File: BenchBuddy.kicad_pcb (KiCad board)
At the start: 4 copper layers, 165.1 x 63.5 mm, 0 parts

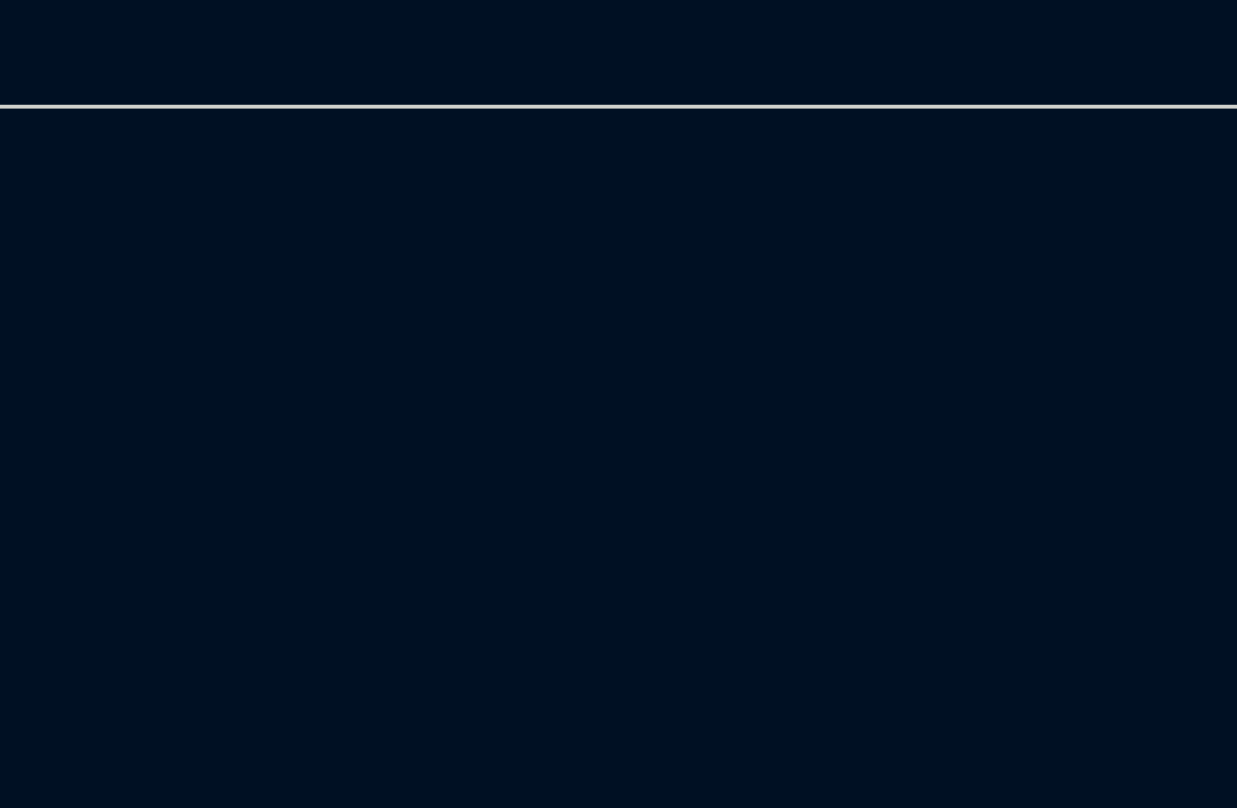
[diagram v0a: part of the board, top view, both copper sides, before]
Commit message: Created Footprints and Placed Relay Module
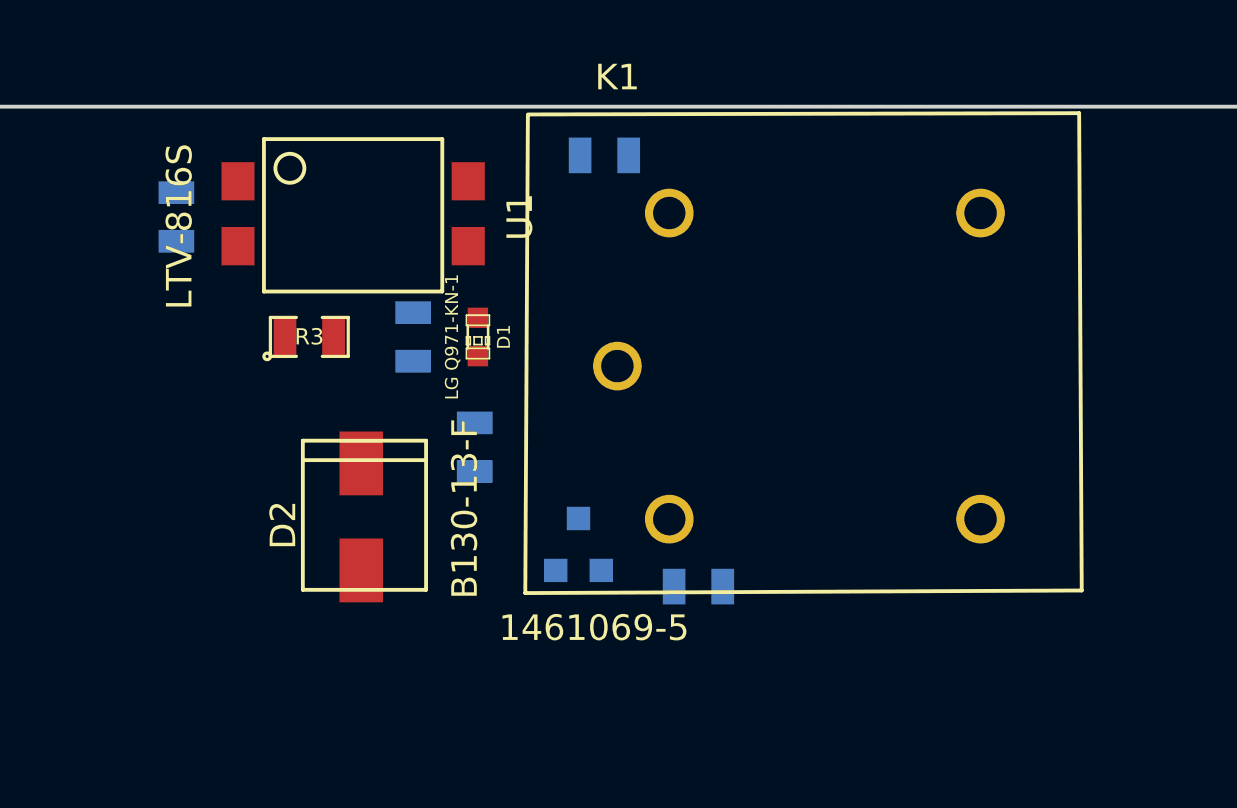
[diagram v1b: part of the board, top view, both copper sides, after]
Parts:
- added D1: LG Q971-KN-1, LED-0603, F.Cu at (264.2, 104.8)
- added D2: B130-13-F, SMA, F.Cu at (259.6, 113.9)
- added K1: 1461069-5, TE-SPDT, F.Cu at (269.6, 105.9)
- added Q1: 2N3904, SOT23EBC, B.Cu at (268.1, 112.9)
- added R1: 500, SM0805, B.Cu at (252.3, 100.1)
- added R2: 200, SM0805, B.Cu at (261.6, 104.8)
- added R3: 0, SM0805, F.Cu at (257.6, 104.8)
- added R4: 100, SM0805, B.Cu at (264.0, 109.1)
- added R5: 0, SM0805, B.Cu at (269.1, 97.7)
- added R6: 0, SM0805, B.Cu at (272.8, 114.6)
- added U1: LTV-816S, 4-SMD, F.Cu at (254.8, 98.7)

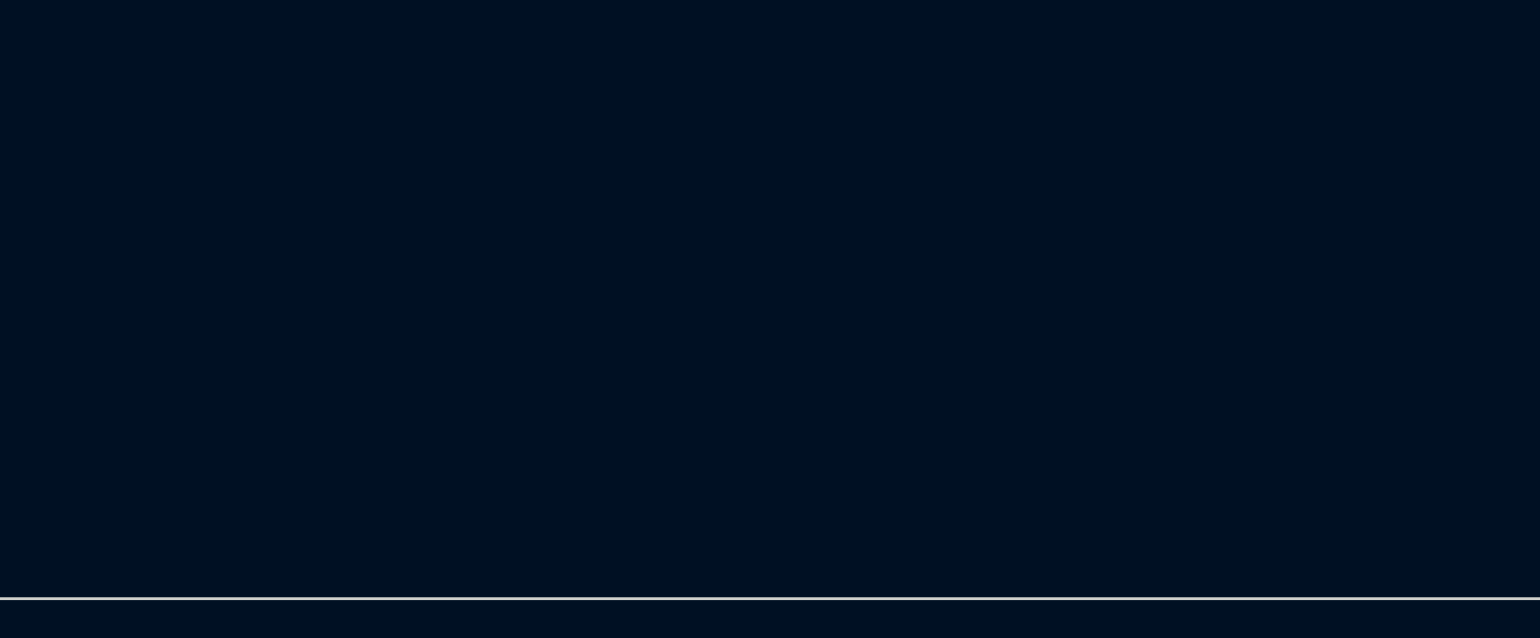
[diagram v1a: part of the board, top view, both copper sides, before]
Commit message: Placing Thermocouple Module Components
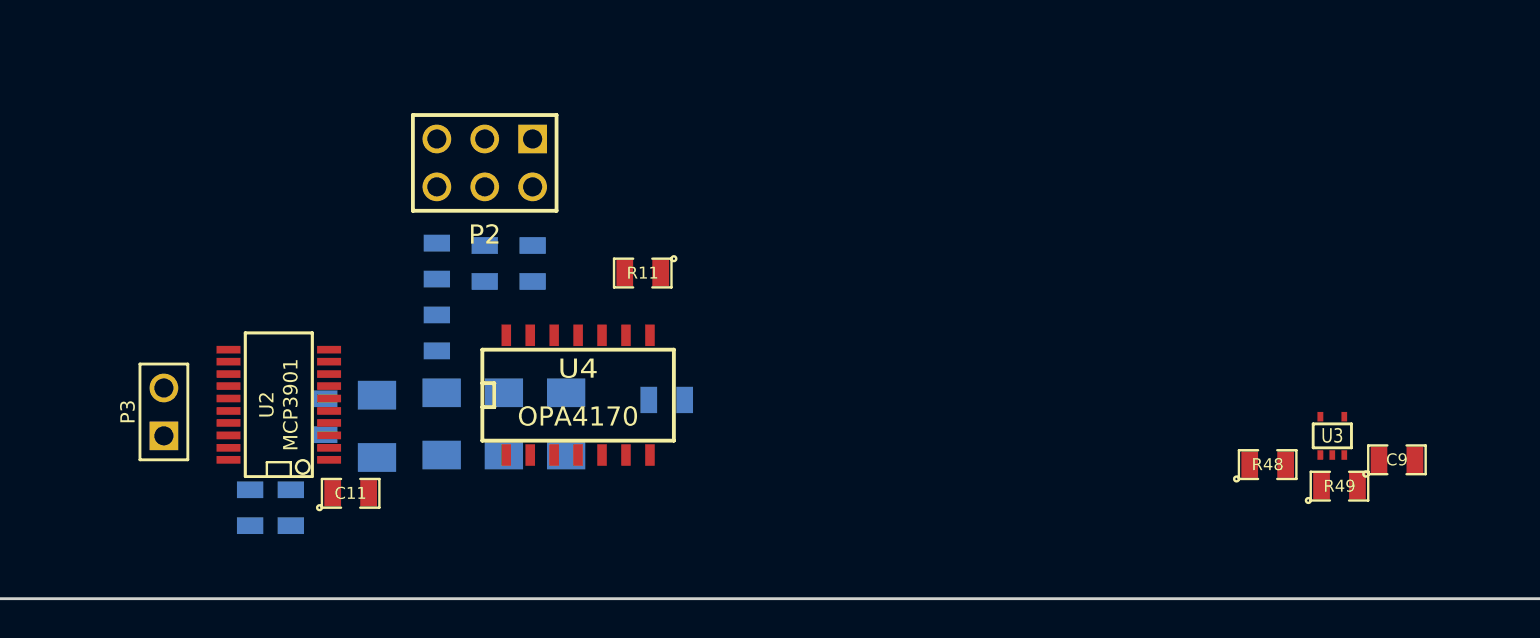
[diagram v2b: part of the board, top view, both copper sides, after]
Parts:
- added C1: C, SM0805, B.Cu at (233.7, 149.6)
- added C10: C, SM0805, B.Cu at (251.8, 148.7)
- added C11: C, SM0805, F.Cu at (235.1, 153.7)
- added C7: C, SM0805, B.Cu at (229.7, 154.4)
- added C8: C, SM0805, B.Cu at (231.9, 154.4)
- added C9: C, SM0805, F.Cu at (290.6, 151.9)
- added P2: CONN_3X2, pin_array_3x2, F.Cu at (242.2, 136.1)
- added P3: CONN_2, PIN_ARRAY_2X1, F.Cu at (225.2, 149.4)
- added R10: R, SM1206, B.Cu at (246.5, 150.0)
- added R11: R, SM0805, F.Cu at (250.6, 142.0)
- added R12: R, SM0805, B.Cu at (244.7, 141.5)
- added R13: R, SM0805, B.Cu at (239.6, 145.2)
- added R44: R, SM0805, B.Cu at (239.6, 141.4)
- added R45: R, SM0805, B.Cu at (242.2, 141.5)
- added R48: 0, SM0805, F.Cu at (283.7, 152.1)
- added R49: 0, SM0805, F.Cu at (287.5, 153.3)
- added R7: R, SM1206, B.Cu at (239.9, 150.0)
- added R8: R, SM1206, B.Cu at (236.5, 150.1)
- added R9: R, SM1206, B.Cu at (243.2, 150.0)
- added U2: MCP3901, SSOP20, F.Cu at (231.3, 149.0)
- added U3: LMT84, SOT353, F.Cu at (287.1, 150.6)
- added U4: OPA4170, SO14N, F.Cu at (247.1, 148.3)

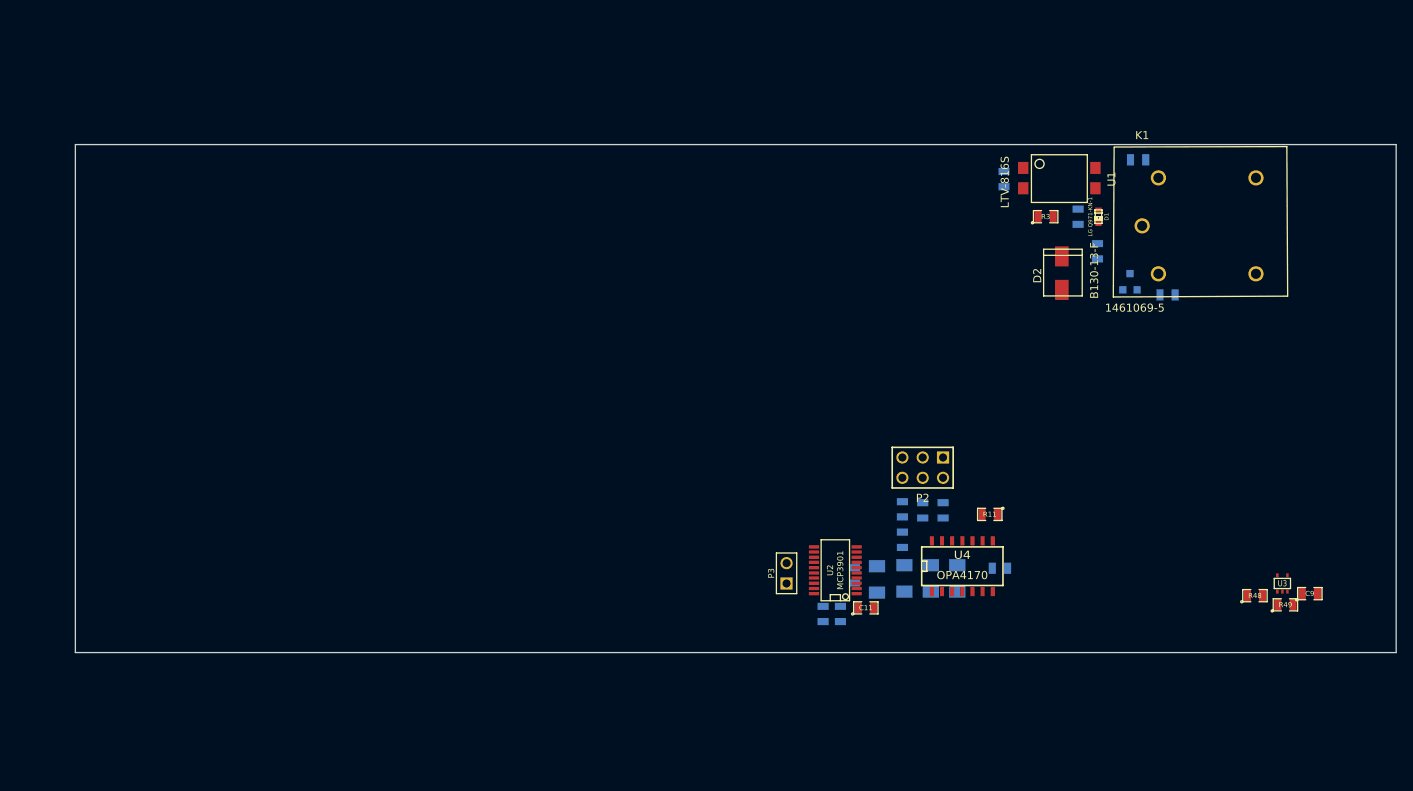
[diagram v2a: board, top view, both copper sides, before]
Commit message: Placing the Terminal Block/ATX Connectors
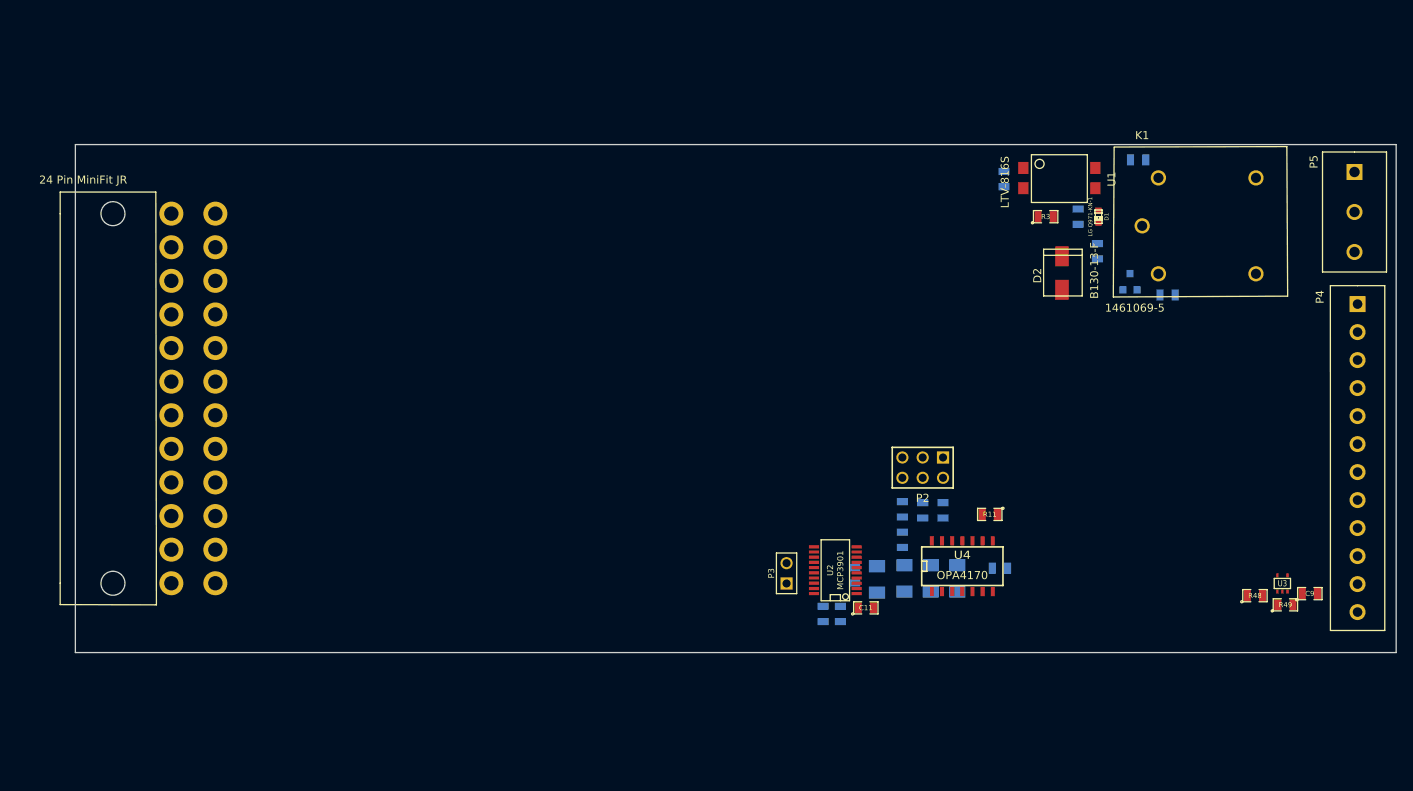
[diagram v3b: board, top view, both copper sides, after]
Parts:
- added P1: 24 Pin MiniFit JR, ATX_Header, F.Cu at (141.0, 104.4)
- added P4: 12 Pin Terminal Block, 12pinTB, F.Cu at (296.5, 115.7)
- added P5: 3 Pin TB, 3pinTB, F.Cu at (296.2, 99.2)
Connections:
- U4 pad 10: (no net) -> /Thermocouple/TC IN +
- U4 pad 12: (no net) -> /Thermocouple/TC IN -

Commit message: Added Arduino Footprint
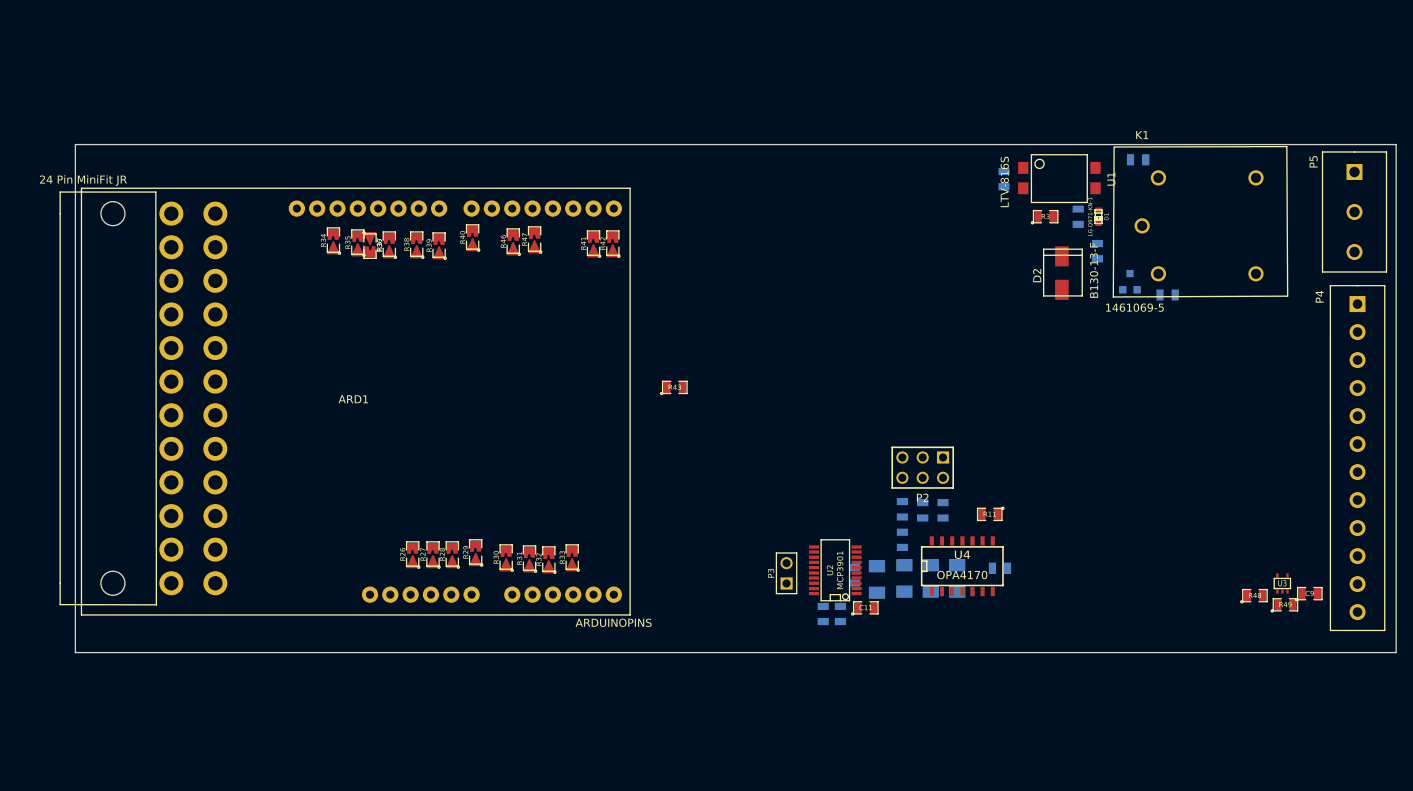
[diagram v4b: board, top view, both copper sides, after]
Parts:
- added ARD1: ARDUINOPINS, Arduino, F.Cu at (171.1, 127.6)
- added R26: R, SM0805-blob, F.Cu at (178.4, 146.9)
- added R27: R, SM0805-blob, F.Cu at (181.0, 146.9)
- added R28: R, SM0805-blob, F.Cu at (183.4, 146.9)
- added R29: R, SM0805-blob, F.Cu at (186.3, 146.7)
- added R30: R, SM0805-blob, F.Cu at (190.1, 147.3)
- added R31: R, SM0805-blob, F.Cu at (193.0, 147.4)
- added R32: R, SM0805-blob, F.Cu at (195.5, 147.6)
- added R33: R, SM0805-blob, F.Cu at (198.4, 147.3)
- added R34: R, SM0805-blob, F.Cu at (168.5, 107.7)
- added R35: R, SM0805-blob, F.Cu at (171.6, 108.0)
- added R36: R, SM0805-blob, F.Cu at (173.1, 108.5)
- added R37: R, SM0805-blob, F.Cu at (175.5, 108.2)
- added R38: R, SM0805-blob, F.Cu at (178.9, 108.2)
- added R39: R, SM0805-blob, F.Cu at (181.7, 108.3)
- added R40: R, SM0805-blob, F.Cu at (185.9, 107.3)
- added R41: R, SM0805-blob, F.Cu at (201.0, 108.1)
- added R42: R, SM0805-blob, F.Cu at (203.5, 108.1)
- added R43: R, SM0805, F.Cu at (211.2, 126.1)
- added R46: R, SM0805-blob, F.Cu at (191.0, 107.8)
- added R47: R, SM0805-blob, F.Cu at (193.7, 107.6)
